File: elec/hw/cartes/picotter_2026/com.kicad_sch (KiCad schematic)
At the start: 6 parts, among them J18 2-1445051-3, U5 TCAN1042DRQ1

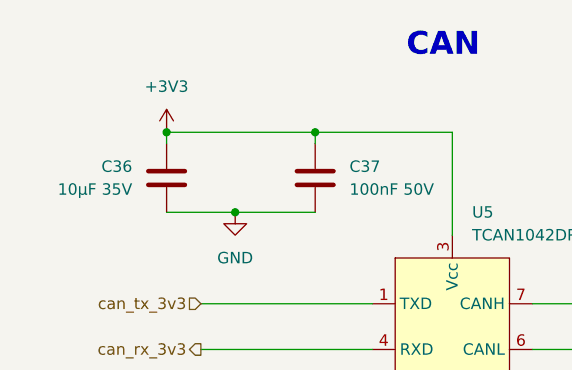
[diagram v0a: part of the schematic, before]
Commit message: picotter: layout almost done (need seriphraphy + layout cleanup)
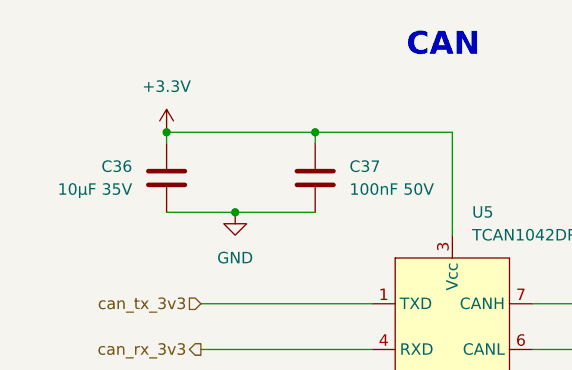
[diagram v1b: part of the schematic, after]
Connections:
- net +3V3 renamed +3.3V
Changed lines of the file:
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@@
-	)
-	(junction
-		(at 29.21 25.4)
-		(diameter 0)
-		(color 0 0 0 0)
 	)
 	(junction
@@
 	(junction
 		(at 36.83 34.29)
+		(diameter 0)
+		(color 0 0 0 0)
+	)
+	(junction
+		(at 29.21 25.4)
 		(diameter 0)
 		(color 0 0 0 0)
@@
 			)
 			(justify right)
+		)
+	)
+	(symbol
+		(lib_id "power:+3.3V")
+		(at 29.21 25.4 0)
+		(unit 1)
+		(exclude_from_sim no)
+		(in_bom yes)
+		(on_board yes)
+		(dnp no)
+		(fields_autoplaced yes)
+		(property "Reference" "#PWR061"
+			(at 29.21 29.21 0)
+			(effects
+				(font
+					(size 1.27 1.27)
+				)
+				(hide yes)
+			)
+		)
+		(property "Value" "+3.3V"
+			(at 29.21 20.32 0)
+			(effects
+				(font
+					(size 1.27 1.27)
+				)
+			)
+		)
+		(property "Footprint" ""
+			(at 29.21 25.4 0)
+			(effects
+				(font
+					(size 1.27 1.27)
+				)
+				(hide yes)
+			)
+		)
+		(property "Datasheet" ""
+			(at 29.21 25.4 0)
+			(effects
+				(font
+					(size 1.27 1.27)
+				)
+				(hide yes)
+			)
+		)
+		(property "Description" "Power symbol creates a global label with name \"+3.3V\""
+			(at 29.21 25.4 0)
+			(effects
+				(font
+					(size 1.27 1.27)
+				)
+				(hide yes)
+			)
+		)
+		(pin "1"
+		)
+		(instances
+			(project ""
+				(path "/a7992a71-8976-4fb0-bae5-4423ba97b789/d36b0a97-acf3-4f06-b6ad-f8f96f789f77"
+					(reference "#PWR061")
+					(unit 1)
+				)
+			)
 		)
 	)
@@
 					(unit 1)
 				)
-			)
-		)
-	)
-	(symbol
-		(lib_id "power:+3V3")
-		(at 29.21 25.4 0)
-		(unit 1)
-		(exclude_from_sim no)
-		(in_bom yes)
-		(on_board yes)
-		(dnp no)
-		(fields_autoplaced yes)
-		(property "Reference" "#PWR061"
-			(at 29.21 29.21 0)
-			(effects
-				(font
-					(size 1.27 1.27)
-				)
-				(hide yes)
-			)
-		)
-		(property "Value" "+3V3"
-			(at 29.21 20.32 0)
-			(effects
-				(font
-					(size 1.27 1.27)
-				)
-			)
-		)
-		(property "Footprint" ""
-			(at 29.21 25.4 0)
-			(effects
-				(font
-					(size 1.27 1.27)
-				)
-				(hide yes)
-			)
-		)
-		(property "Datasheet" ""
-			(at 29.21 25.4 0)
-			(effects
-				(font
-					(size 1.27 1.27)
-				)
-				(hide yes)
-			)
-		)
-		(property "Description" "Power symbol creates a global label with name \"+3V3\""
-			(at 29.21 25.4 0)
-			(effects
-				(font
-					(size 1.27 1.27)
-				)
-				(hide yes)
-			)
-		)
-		(pin "1"
-		)
-		(instances
-			(project "picotter_2026"
-				(path "/a7992a71-8976-4fb0-bae5-4423ba97b789/d36b0a97-acf3-4f06-b6ad-f8f96f789f77"
-					(reference "#PWR061")
-					(unit 1)
-				)
